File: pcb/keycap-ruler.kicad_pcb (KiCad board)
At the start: 2 copper layers, 200 x 45 mm, 0 parts

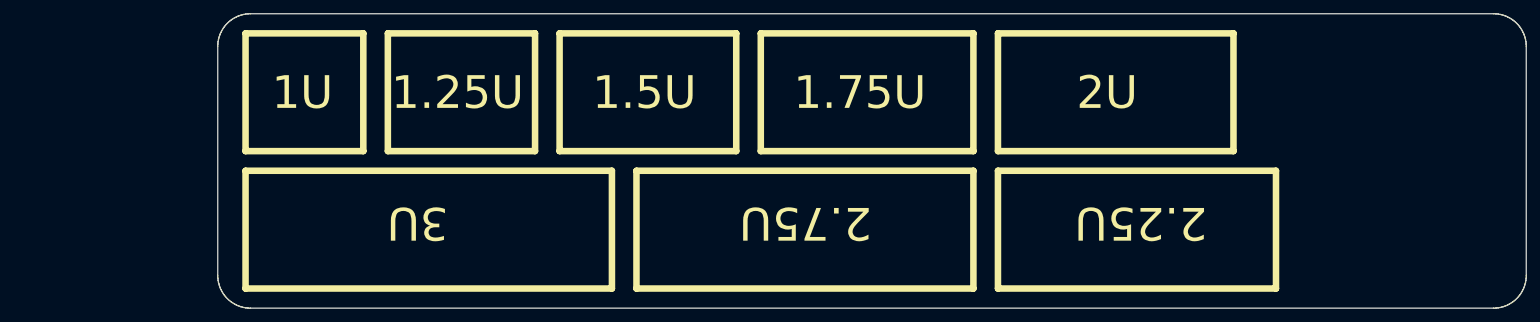
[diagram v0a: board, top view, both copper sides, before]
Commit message: Add switch sockets and logo
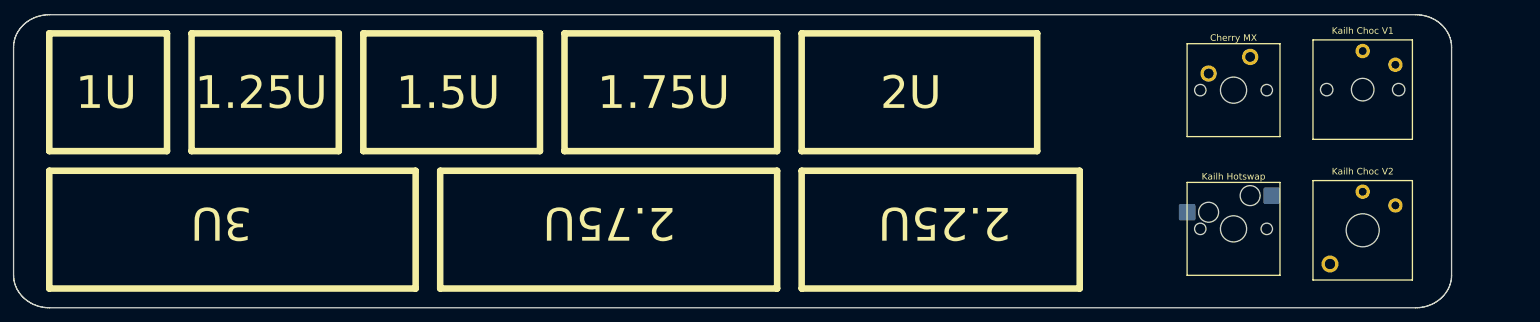
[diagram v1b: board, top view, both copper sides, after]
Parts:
- added Cherry MX: SW_Cherry_MX_PCB_1.00u, Switch_Keyboard_Cherry_MX:SW_Cherry_MX_PCB_1.00u, F.Cu at (225.3, 71.7)
- added Kailh Choc V1: SW_Kailh_Choc_V1_1.00u, Switch_Keyboard_Kailh:SW_Kailh_Choc_V1_1.00u, F.Cu at (245.0, 71.6)
- added Kailh Choc V2: SW_Kailh_Choc_V2_1.00u, Switch_Keyboard_Kailh:SW_Kailh_Choc_V2_1.00u, F.Cu at (245.0, 93.1)
- added Kailh Hotswap: SW_Hotswap_Kailh_MX_1.00u, Switch_Keyboard_Hotswap_Kailh:SW_Hotswap_Kailh_MX_1.00u, F.Cu at (225.3, 92.9)
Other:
- board size 200 x 45 mm -> 219.8 x 44.8 mm
- board text added: "Designed in Bristol, UK by richdawe"
- board text added: "keycap ruler"
